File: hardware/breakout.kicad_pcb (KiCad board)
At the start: 2 copper layers, 40.3 x 50 mm, 11 parts, among them J1 Conn_01x18_Male, J2 Conn_Coaxial, J3 Conn_01x18_Male, J4 Conn_Coaxial, SW1 SW_Push, U1 RFM95W-915S2

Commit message: add NSS symbol to silkscreen
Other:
- board text added: "NSS"

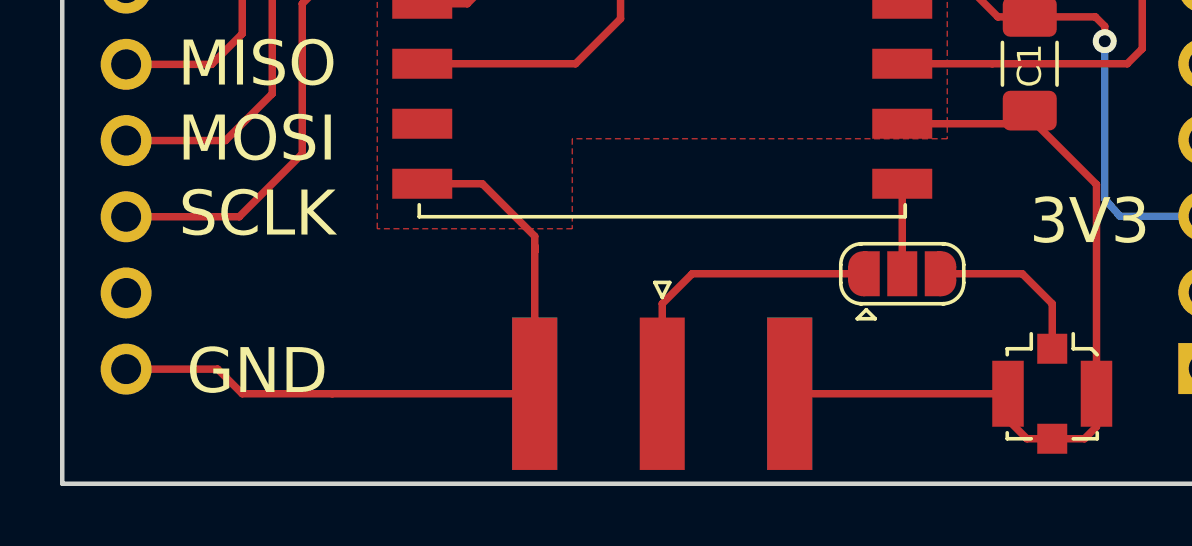
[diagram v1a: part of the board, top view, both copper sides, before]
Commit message: fix the footprint of the antenna connector
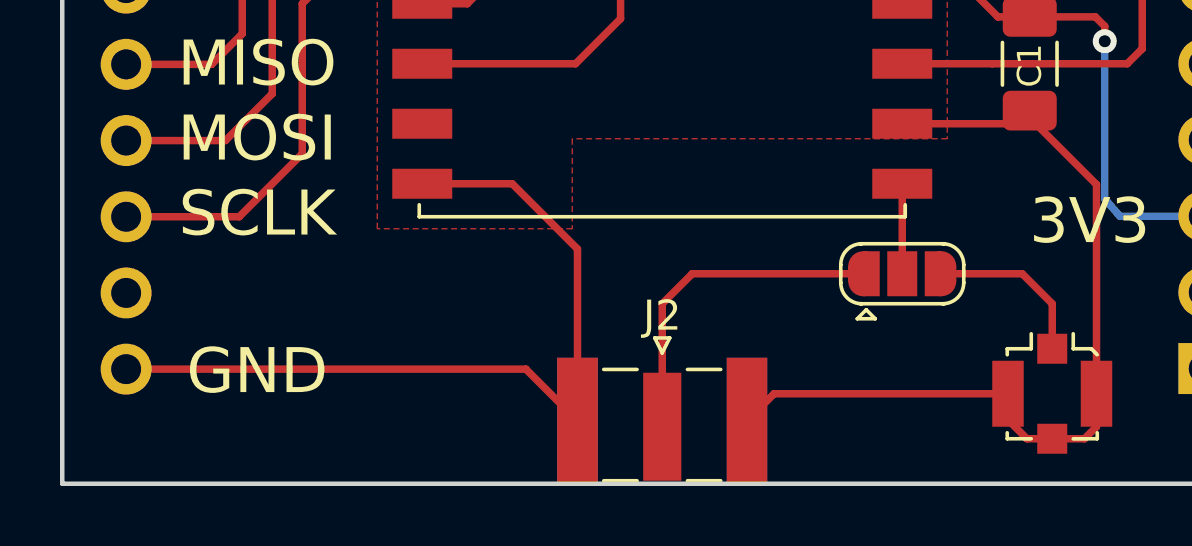
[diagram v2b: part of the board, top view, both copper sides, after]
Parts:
- J2: footprint KiCad/kicad-footprints/Connector_Coaxial.pretty:SMA_Amphenol_132289_EdgeMount -> KiCad/kicad-footprints/Connector_Coaxial.pretty:SMA_Samtec_SMA-J-P-X-ST-EM1_EdgeMount
- moved J2 0.90 mm to (145.0, 122.9), turned to 0 degrees
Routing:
- net GND: track 50.9 -> 56.4 mm
- net Net-(J2-Pad1): track 10.1 -> 11.2 mm
